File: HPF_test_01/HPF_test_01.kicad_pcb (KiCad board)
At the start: 2 copper layers, 11 parts, among them J1 BNC5-J-P-GN-RA-BH2D, J2 Conn_01x01, J3 Conn_01x01, T1 GT07-110-013, U1 SL1002A600SP

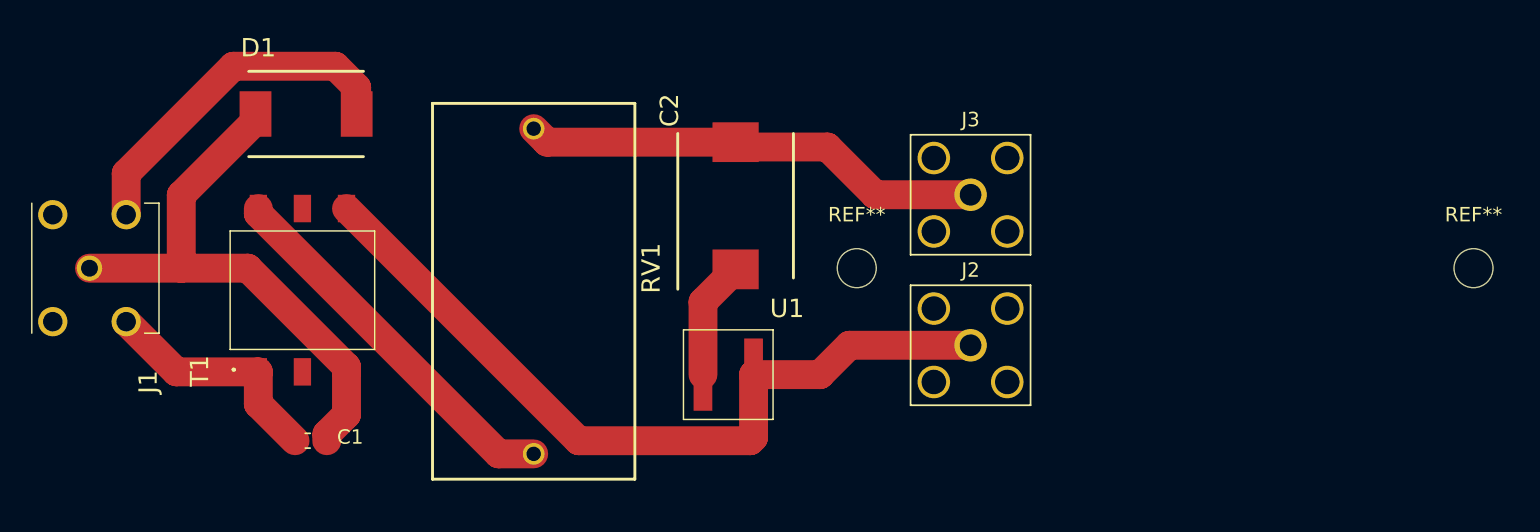
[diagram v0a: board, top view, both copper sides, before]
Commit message: Added modified GT07 footprint to accept T3001NL transformer
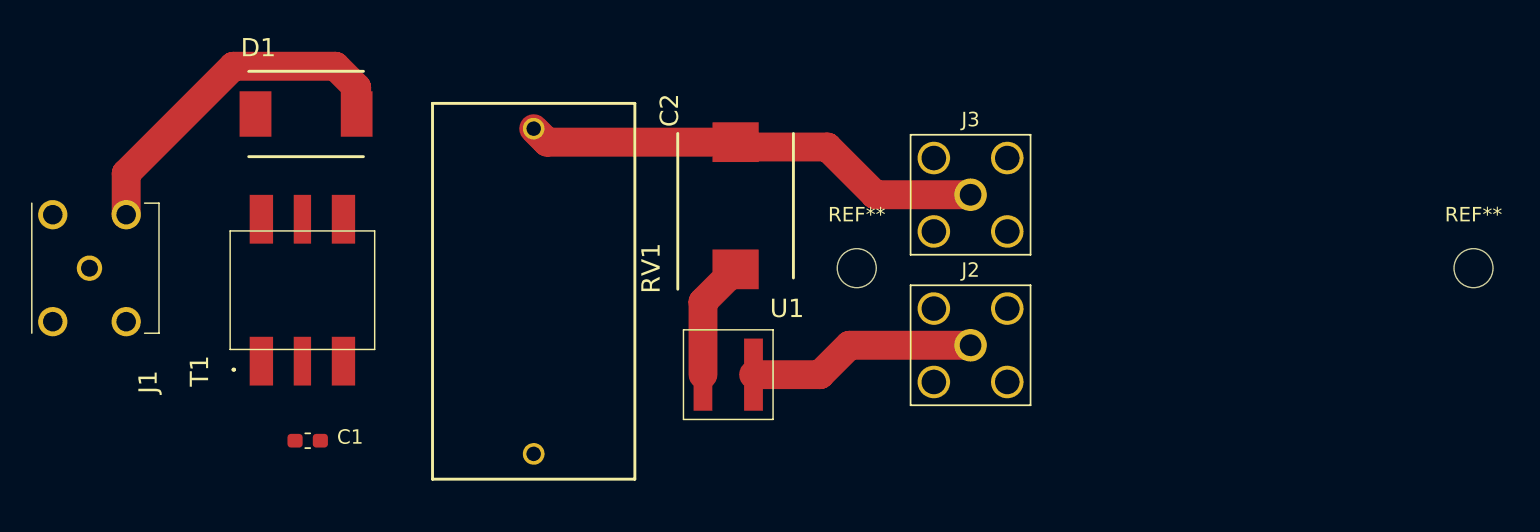
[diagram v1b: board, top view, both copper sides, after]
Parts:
- T1: footprint Kicad-GT07-models:GT07110013 -> GT07-110-013-Modifed:GT07110013
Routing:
- net Net-(J2-Pad1): track 55.1 -> 15.9 mm
- net Net-(C1-Pad2): track 39.1 -> 0.00 mm
- net Net-(C2-Pad2): track 26.3 -> 0.00 mm
- net Net-(C1-Pad1): track 40.7 -> 24.3 mm
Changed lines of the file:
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@@
     (thickness 1.6)
     (drawings 0)
-    (tracks 37)
+    (tracks 16)
     (zones 0)
     (modules 11)
@@
     (add_net "Net-(T1-Pad5)")
   )
+  (module GT07-110-013-Modifed:GT07110013 (layer F.Cu)
+    (at 103.378 88.9 180)
+    (descr GT07-110-013-3)
+    (tags Transformer)
+    (attr smd)
+    (fp_text reference T1 (at 7.112 -5.588 270) (layer F.SilkS)
+      (effects (font (size 1.27 1.27) (thickness 0.254)))
+    )
+    (fp_text value GT07-110-013 (at -7.62 0 270) (layer F.SilkS) hide
+      (effects (font (size 1.27 1.27) (thickness 0.254)))
+    )
+    (fp_text user %R (at 7.112 -5.588 270) (layer F.Fab)
+      (effects (font (size 1.27 1.27) (thickness 0.254)))
+    )
+    (fp_arc (start 4.75 -5.5) (end 4.7 -5.5) (angle -180) (layer F.SilkS) (width 0.2))
+    (fp_arc (start 4.75 -5.5) (end 4.8 -5.5) (angle -180) (layer F.SilkS) (width 0.2))
+    (fp_arc (start 4.75 -5.5) (end 4.7 -5.5) (angle -180) (layer F.SilkS) (width 0.2))
+    (fp_line (start 4.7 -5.5) (end 4.7 -5.5) (layer F.SilkS) (width 0.2))
+    (fp_line (start 4.8 -5.5) (end 4.8 -5.5) (layer F.SilkS) (width 0.2))
+    (fp_line (start 4.7 -5.5) (end 4.7 -5.5) (layer F.SilkS) (width 0.2))
+    (fp_line (start -6 7.6) (end -6 -7.6) (layer F.CrtYd) (width 0.1))
+    (fp_line (start 6 7.6) (end -6 7.6) (layer F.CrtYd) (width 0.1))
+    (fp_line (start 6 -7.6) (end 6 7.6) (layer F.CrtYd) (width 0.1))
+    (fp_line (start -6 -7.6) (end 6 -7.6) (layer F.CrtYd) (width 0.1))
+    (fp_line (start -5 4.1) (end -5 -4.1) (layer F.SilkS) (width 0.1))
+    (fp_line (start 5 4.1) (end -5 4.1) (layer F.SilkS) (width 0.1))
+    (fp_line (start 5 -4.1) (end 5 4.1) (layer F.SilkS) (width 0.1))
+    (fp_line (start -5 -4.1) (end 5 -4.1) (layer F.SilkS) (width 0.1))
+    (fp_line (start -5 -4.1) (end -5 4.1) (layer F.Fab) (width 0.2))
+    (fp_line (start 5 -4.1) (end -5 -4.1) (layer F.Fab) (width 0.2))
+    (fp_line (start 5 4.1) (end 5 -4.1) (layer F.Fab) (width 0.2))
+    (fp_line (start -5 4.1) (end 5 4.1) (layer F.Fab) (width 0.2))
+    (pad 1 smd rect (at 2.84 -4.91 180) (size 1.62 3.375) (layers F.Cu F.Paste F.Mask)
+      (net 2 "Net-(C1-Pad1)"))
+    (pad 2 smd rect (at 0 -4.91 180) (size 1.2 3.375) (layers F.Cu F.Paste F.Mask)
+      (net 8 "Net-(T1-Pad2)"))
+    (pad 3 smd rect (at -2.84 -4.91 180) (size 1.62 3.375) (layers F.Cu F.Paste F.Mask)
+      (net 1 "Net-(C1-Pad2)"))
+    (pad 4 smd rect (at -2.84 4.91 180) (size 1.62 3.375) (layers F.Cu F.Paste F.Mask)
+      (net 5 "Net-(J2-Pad1)"))
+    (pad 5 smd rect (at 0 4.91 180) (size 1.2 3.375) (layers F.Cu F.Paste F.Mask)
+      (net 7 "Net-(T1-Pad5)"))
+    (pad 6 smd rect (at 2.84 4.91 180) (size 1.62 3.375) (layers F.Cu F.Paste F.Mask)
+      (net 3 "Net-(C2-Pad2)"))
+  )
   (module MountingHole:MountingHole_2.7mm_M2.5 (layer F.Cu)
     (at 184.404 87.376)
@@
       (rotate (xyz 0 0 0))
     )
-  )
-  (module Kicad-GT07-models:GT07110013 (layer F.Cu)
-    (at 103.378 88.9 180)
-    (descr GT07-110-013-3)
-    (tags Transformer)
-    (attr smd)
-    (fp_text reference T1 (at 7.112 -5.588 270) (layer F.SilkS)
-      (effects (font (size 1.27 1.27) (thickness 0.254)))
-    )
-    (fp_text value GT07-110-013 (at -7.62 0 270) (layer F.SilkS) hide
-      (effects (font (size 1.27 1.27) (thickness 0.254)))
-    )
-    (fp_line (start -5 4.1) (end 5 4.1) (layer F.Fab) (width 0.2))
-    (fp_line (start 5 4.1) (end 5 -4.1) (layer F.Fab) (width 0.2))
-    (fp_line (start 5 -4.1) (end -5 -4.1) (layer F.Fab) (width 0.2))
-    (fp_line (start -5 -4.1) (end -5 4.1) (layer F.Fab) (width 0.2))
-    (fp_line (start -5 -4.1) (end 5 -4.1) (layer F.SilkS) (width 0.1))
-    (fp_line (start 5 -4.1) (end 5 4.1) (layer F.SilkS) (width 0.1))
-    (fp_line (start 5 4.1) (end -5 4.1) (layer F.SilkS) (width 0.1))
-    (fp_line (start -5 4.1) (end -5 -4.1) (layer F.SilkS) (width 0.1))
-    (fp_line (start -6 -7.6) (end 6 -7.6) (layer F.CrtYd) (width 0.1))
-    (fp_line (start 6 -7.6) (end 6 7.6) (layer F.CrtYd) (width 0.1))
-    (fp_line (start 6 7.6) (end -6 7.6) (layer F.CrtYd) (width 0.1))
-    (fp_line (start -6 7.6) (end -6 -7.6) (layer F.CrtYd) (width 0.1))
-    (fp_line (start 4.7 -5.5) (end 4.7 -5.5) (layer F.SilkS) (width 0.2))
-    (fp_line (start 4.8 -5.5) (end 4.8 -5.5) (layer F.SilkS) (width 0.2))
-    (fp_line (start 4.7 -5.5) (end 4.7 -5.5) (layer F.SilkS) (width 0.2))
-    (fp_arc (start 4.75 -5.5) (end 4.7 -5.5) (angle -180) (layer F.SilkS) (width 0.2))
-    (fp_arc (start 4.75 -5.5) (end 4.8 -5.5) (angle -180) (layer F.SilkS) (width 0.2))
-    (fp_arc (start 4.75 -5.5) (end 4.7 -5.5) (angle -180) (layer F.SilkS) (width 0.2))
-    (fp_text user %R (at 7.112 -5.588 270) (layer F.Fab)
-      (effects (font (size 1.27 1.27) (thickness 0.254)))
-    )
-    (pad 6 smd rect (at 3.05 5.65 180) (size 1.2 1.9) (layers F.Cu F.Paste F.Mask)
-      (net 3 "Net-(C2-Pad2)"))
-    (pad 5 smd rect (at 0 5.65 180) (size 1.2 1.9) (layers F.Cu F.Paste F.Mask)
-      (net 7 "Net-(T1-Pad5)"))
-    (pad 4 smd rect (at -3.05 5.65 180) (size 1.2 1.9) (layers F.Cu F.Paste F.Mask)
-      (net 5 "Net-(J2-Pad1)"))
-    (pad 3 smd rect (at -3.05 -5.65 180) (size 1.2 1.9) (layers F.Cu F.Paste F.Mask)
-      (net 1 "Net-(C1-Pad2)"))
-    (pad 2 smd rect (at 0 -5.65 180) (size 1.2 1.9) (layers F.Cu F.Paste F.Mask)
-      (net 8 "Net-(T1-Pad2)"))
-    (pad 1 smd rect (at 3.05 -5.65 180) (size 1.2 1.9) (layers F.Cu F.Paste F.Mask)
-      (net 2 "Net-(C1-Pad1)"))
   )
   (module VP4032K122R300_kicad:CAPPM10080X500N (layer F.Cu)
@@
     )
   )
-  (segment (start 94.996 87.376) (end 88.646 87.376) (width 2) (layer F.Cu) (net 1))
-  (segment (start 100.132 76.708) (end 100.132 77.183) (width 2) (layer F.Cu) (net 1))
-  (segment (start 100.132 77.183) (end 94.996 82.319) (width 2) (layer F.Cu) (net 1))
-  (segment (start 94.996 82.319) (end 94.996 87.376) (width 2) (layer F.Cu) (net 1))
-  (segment (start 106.428 94.55) (end 106.428 94.2) (width 2) (layer F.Cu) (net 1))
-  (segment (start 99.604 87.376) (end 94.996 87.376) (width 2) (layer F.Cu) (net 1))
-  (segment (start 106.428 94.2) (end 99.604 87.376) (width 2) (layer F.Cu) (net 1))
-  (segment (start 105.070008 98.863992) (end 105.070008 99.314) (width 2) (layer F.Cu) (net 1))
-  (segment (start 106.428 97.506) (end 105.070008 98.863992) (width 2) (layer F.Cu) (net 1))
-  (segment (start 106.428 94.55) (end 106.428 97.506) (width 2) (layer F.Cu) (net 1))
   (segment (start 107.132 76.708) (end 107.132 74.874) (width 2) (layer F.Cu) (net 2))
   (segment (start 107.132 74.874) (end 105.664 73.406) (width 2) (layer F.Cu) (net 2))
@@
   (segment (start 105.664 73.406) (end 98.598998 73.406) (width 2) (layer F.Cu) (net 2))
   (segment (start 98.598998 73.406) (end 91.186 80.818998) (width 2) (layer F.Cu) (net 2))
-  (segment (start 100.328 96.772) (end 102.87 99.314) (width 2) (layer F.Cu) (net 2))
-  (segment (start 100.328 94.55) (end 100.328 96.772) (width 2) (layer F.Cu) (net 2))
-  (segment (start 94.66 94.55) (end 91.186 91.076) (width 2) (layer F.Cu) (net 2))
-  (segment (start 100.328 94.55) (end 94.66 94.55) (width 2) (layer F.Cu) (net 2))
-  (segment (start 116.952 100.224) (end 119.38 100.224) (width 2) (layer F.Cu) (net 3))
-  (segment (start 100.328 83.6) (end 116.952 100.224) (width 2) (layer F.Cu) (net 3))
-  (segment (start 100.328 83.25) (end 100.328 83.6) (width 2) (layer F.Cu) (net 3))
   (segment (start 120.314 78.658) (end 119.38 77.724) (width 2) (layer F.Cu) (net 4))
   (segment (start 133.35 78.658) (end 120.314 78.658) (width 2) (layer F.Cu) (net 4))
@@
   (segment (start 133.686 78.994) (end 133.35 78.658) (width 2) (layer F.Cu) (net 4))
   (segment (start 139.7 78.994) (end 133.686 78.994) (width 2) (layer F.Cu) (net 4))
-  (segment (start 134.592 94.742) (end 134.592 99.088) (width 2) (layer F.Cu) (net 5))
-  (segment (start 134.592 99.088) (end 134.366 99.314) (width 2) (layer F.Cu) (net 5))
-  (segment (start 122.492 99.314) (end 106.428 83.25) (width 2) (layer F.Cu) (net 5))
-  (segment (start 134.366 99.314) (end 122.492 99.314) (width 2) (layer F.Cu) (net 5))
   (segment (start 149.606 92.71) (end 141.224 92.71) (width 2) (layer F.Cu) (net 5))
   (segment (start 139.192 94.742) (end 134.592 94.742) (width 2) (layer F.Cu) (net 5))

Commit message: Added Banana Jack footprint
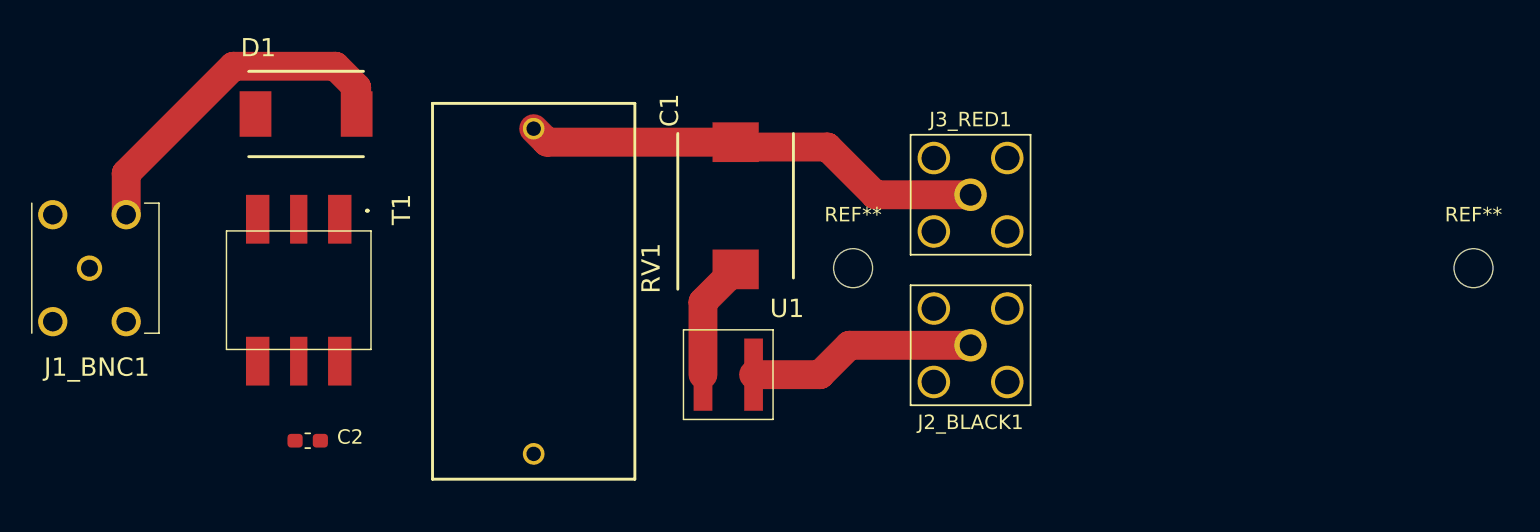
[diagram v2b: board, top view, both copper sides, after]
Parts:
- moved T1 0.25 mm to (103.1, 88.9), turned to 0 degrees
- moved REF** 0.25 mm to (141.5, 87.4)
- renumbered C2 to C1, C1 to C2, J1 to J1_BNC1, J2 to J2_BLACK1, J3 to J3_RED1

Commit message: Updated Layout, added screenshots
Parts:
- removed the REF** at (184.4, 87.4)
- removed the REF** at (141.5, 87.4)
- added REF**: MountingHole_2.2mm_M2_Pad, MountingHole:MountingHole_2.2mm_M2_Pad, F.Cu at (100.1, 99.3)
- added REF**: MountingHole_2.2mm_M2_Pad, MountingHole:MountingHole_2.2mm_M2_Pad, F.Cu at (100.1, 78.7)
- added REF**: MountingHole_2.2mm_M2_Pad, MountingHole:MountingHole_2.2mm_M2_Pad, F.Cu at (141.5, 91.2)
- BLACK: renamed from J2_BLACK1; footprint Connector_Coaxial:SMA_Amphenol_132203-12_Horizontal -> Banana_Jack_Safety_Right_Angle_73099:Banana_Jack_S_RA_73099
- RED: renamed from J3_RED1; footprint Connector_Coaxial:SMA_Amphenol_132203-12_Horizontal -> Banana_Jack_Safety_Right_Angle_73099:Banana_Jack_S_RA_73099
- moved C2 17.0 mm to (107.4, 82.7), turned to 270 degrees
- moved TVS 12.1 mm to (113.8, 83.3)
- moved T1 11.6 mm to (112.8, 95.2)
- moved BNC 11.5 mm to (100.1, 88.9)
- moved C1 8.13 mm to (127.5, 77.7)
- moved GDT 7.97 mm to (139.7, 98.8), turned to 270 degrees
- moved MOV 7.40 mm to (140.5, 81.0)
- moved BLACK 4.20 mm to (151.4, 96.5), turned to 0 degrees
- moved RED 1.93 mm to (151.4, 81.5), turned to 0 degrees
- renumbered J1_BNC1 to BNC, U1 to GDT, RV1 to MOV, D1 to TVS
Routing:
- net Net-(J2_BLACK1-Pad1): track 15.9 -> 48.6 mm
- net Net-(C2-Pad1): track 24.3 -> 44.5 mm
- net Net-(C2-Pad2): track 0.00 -> 19.7 mm
- net Net-(C1-Pad2): track 0.00 -> 11.9 mm
- net Net-(RV1-Pad1): track 8.22 -> 14.5 mm
- net Net-(C1-Pad1): track 32.1 -> 26.4 mm
- added copper zone on F.Cu, net (none)
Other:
- board outline added: 69.1 x 29.2 mm
- board text added: "HPF rev.01 jan2022 //keyudits"

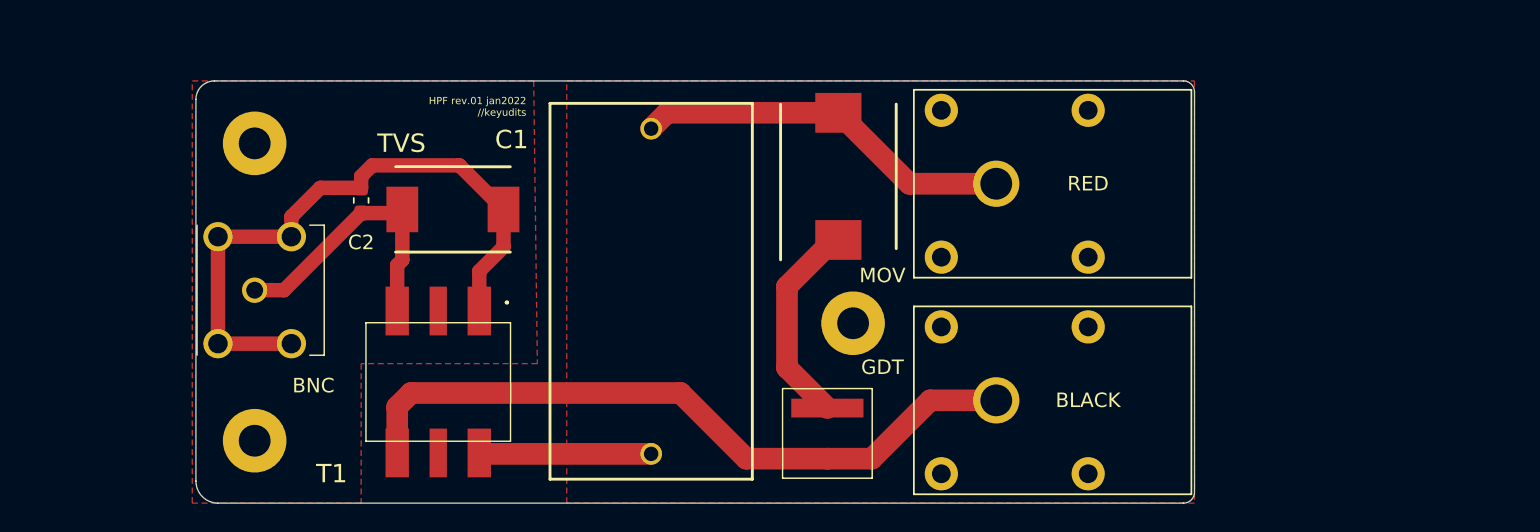
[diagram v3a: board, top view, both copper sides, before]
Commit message: PCB: Added traces, edgecuts, & accurate bananajack footprint. SPICE: Added spice data folders & updated eeschema simulation. 3D: Added 3d render folder and initial board render
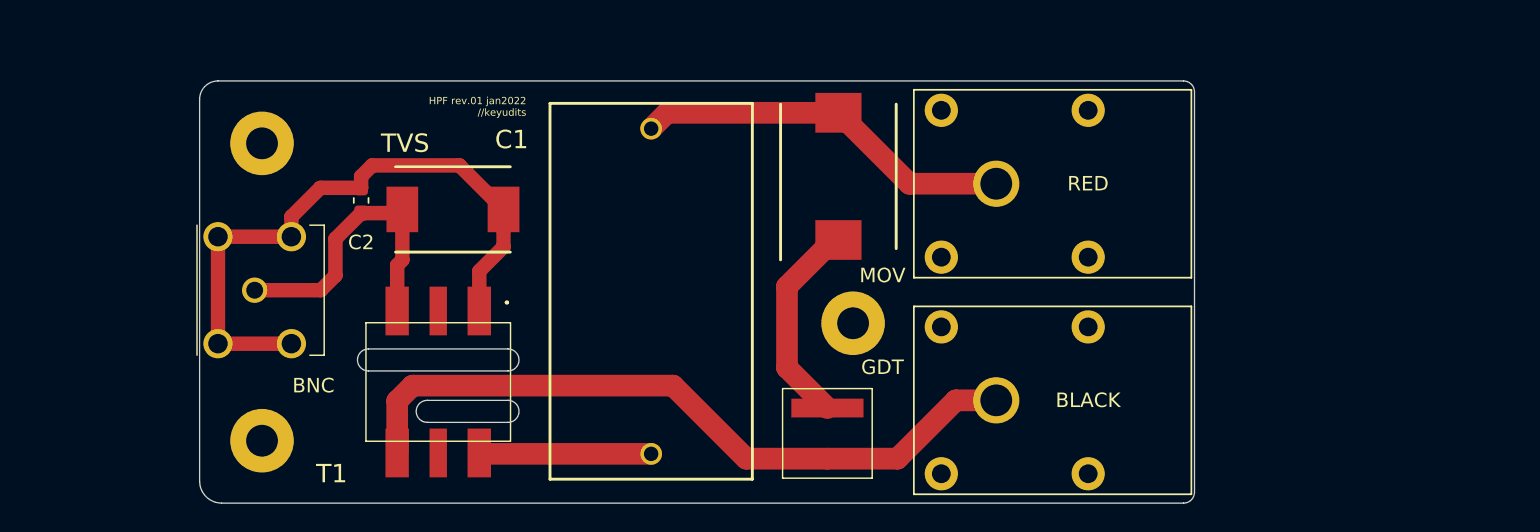
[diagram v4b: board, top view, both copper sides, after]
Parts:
- removed the REF** at (100.1, 99.3)
- removed the REF** at (100.1, 78.7)
- added REF**: MountingHole_2.2mm_M2_Pad, MountingHole:MountingHole_2.2mm_M2_Pad, F.Cu at (100.6, 99.3)
- added REF**: MountingHole_2.2mm_M2_Pad, MountingHole:MountingHole_2.2mm_M2_Pad, F.Cu at (100.6, 78.7)
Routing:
- net Net-(C2-Pad2): track 19.7 -> 21.2 mm
- net Net-(J2_BLACK1-Pad1): track 48.6 -> 49.2 mm
- removed copper zone on F.Cu, net (none)
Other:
- board size 69.1 x 29.2 mm -> 68.8 x 29.2 mm
- board text added: "non-plated cutout"
